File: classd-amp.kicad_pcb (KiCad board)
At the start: 4 copper layers, 80 parts, among them J1 POWER, Q1 IRF540N, Q2 IRF540N, Q3 IRF540N, Q4 IRF540N, Q5 2N3906, Q6 2N3904, U1 TL072, U2 TL072, U3 NE555P, U4 LT1016, U5 IR2184, U6 IR2184, U7 LM7812_TO220, U8 LM7805_TO220, U9 LM358

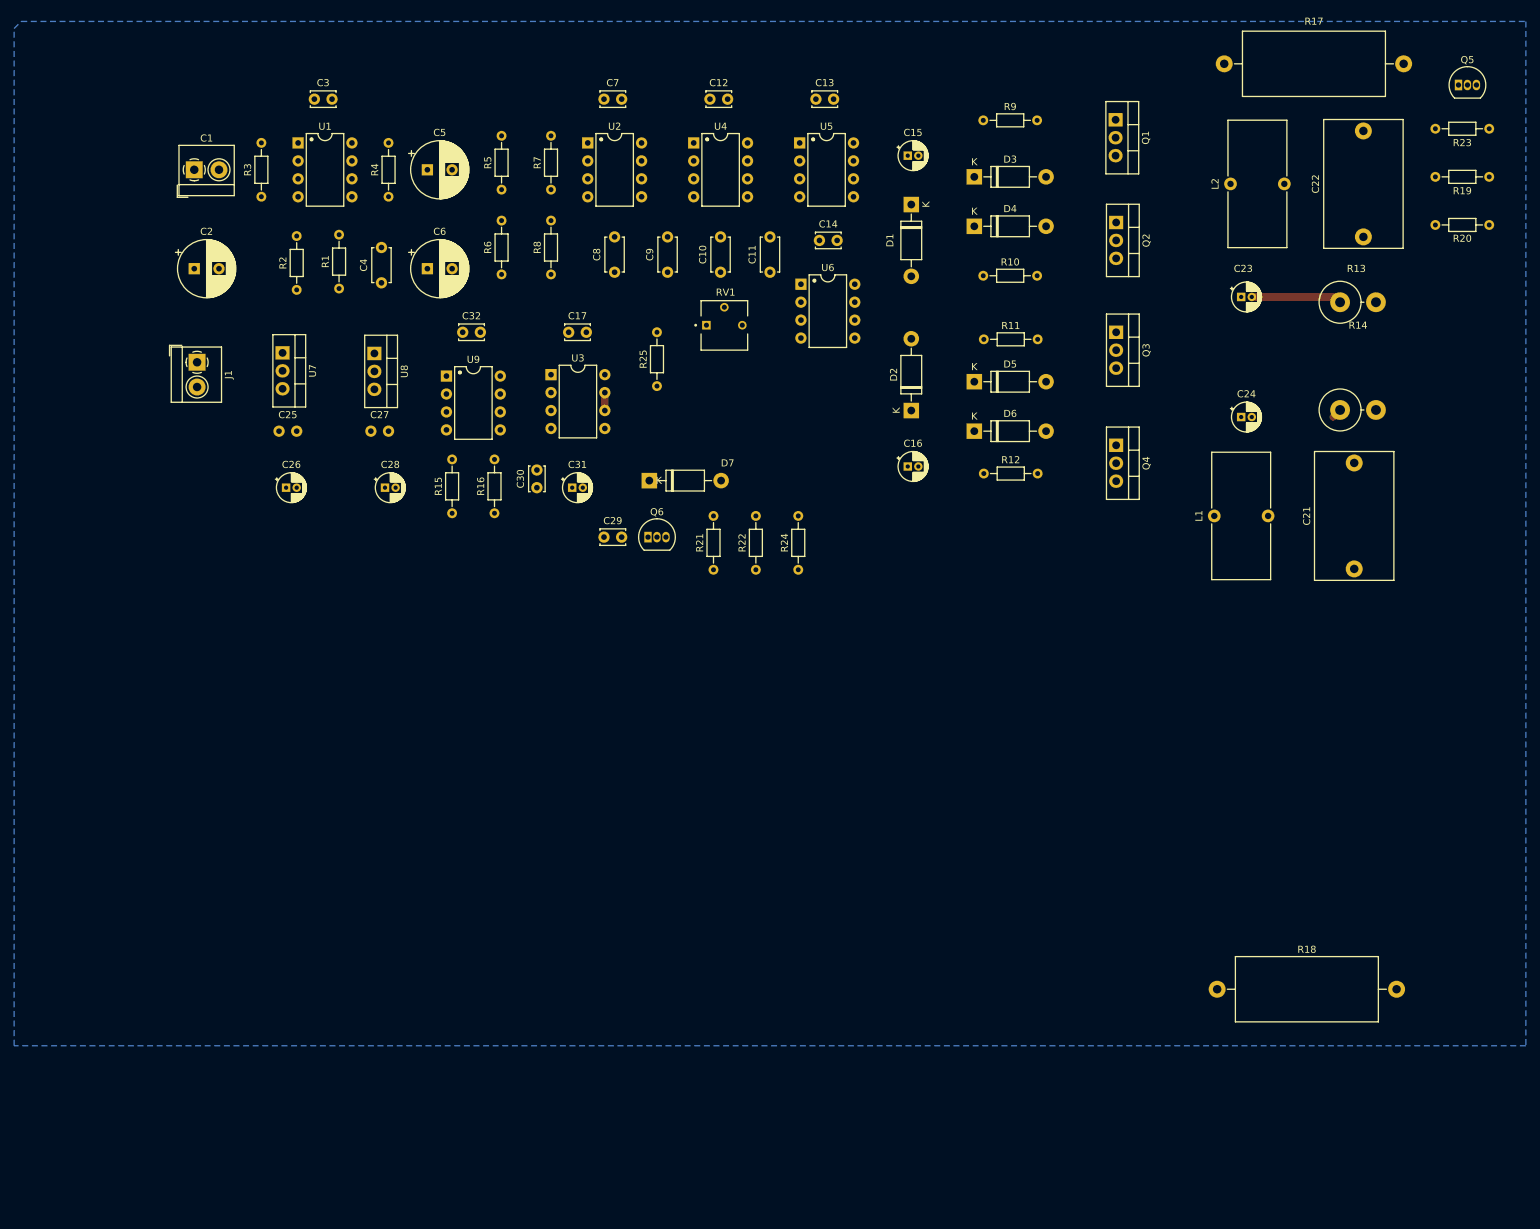
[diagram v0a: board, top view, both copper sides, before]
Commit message: Added right channel
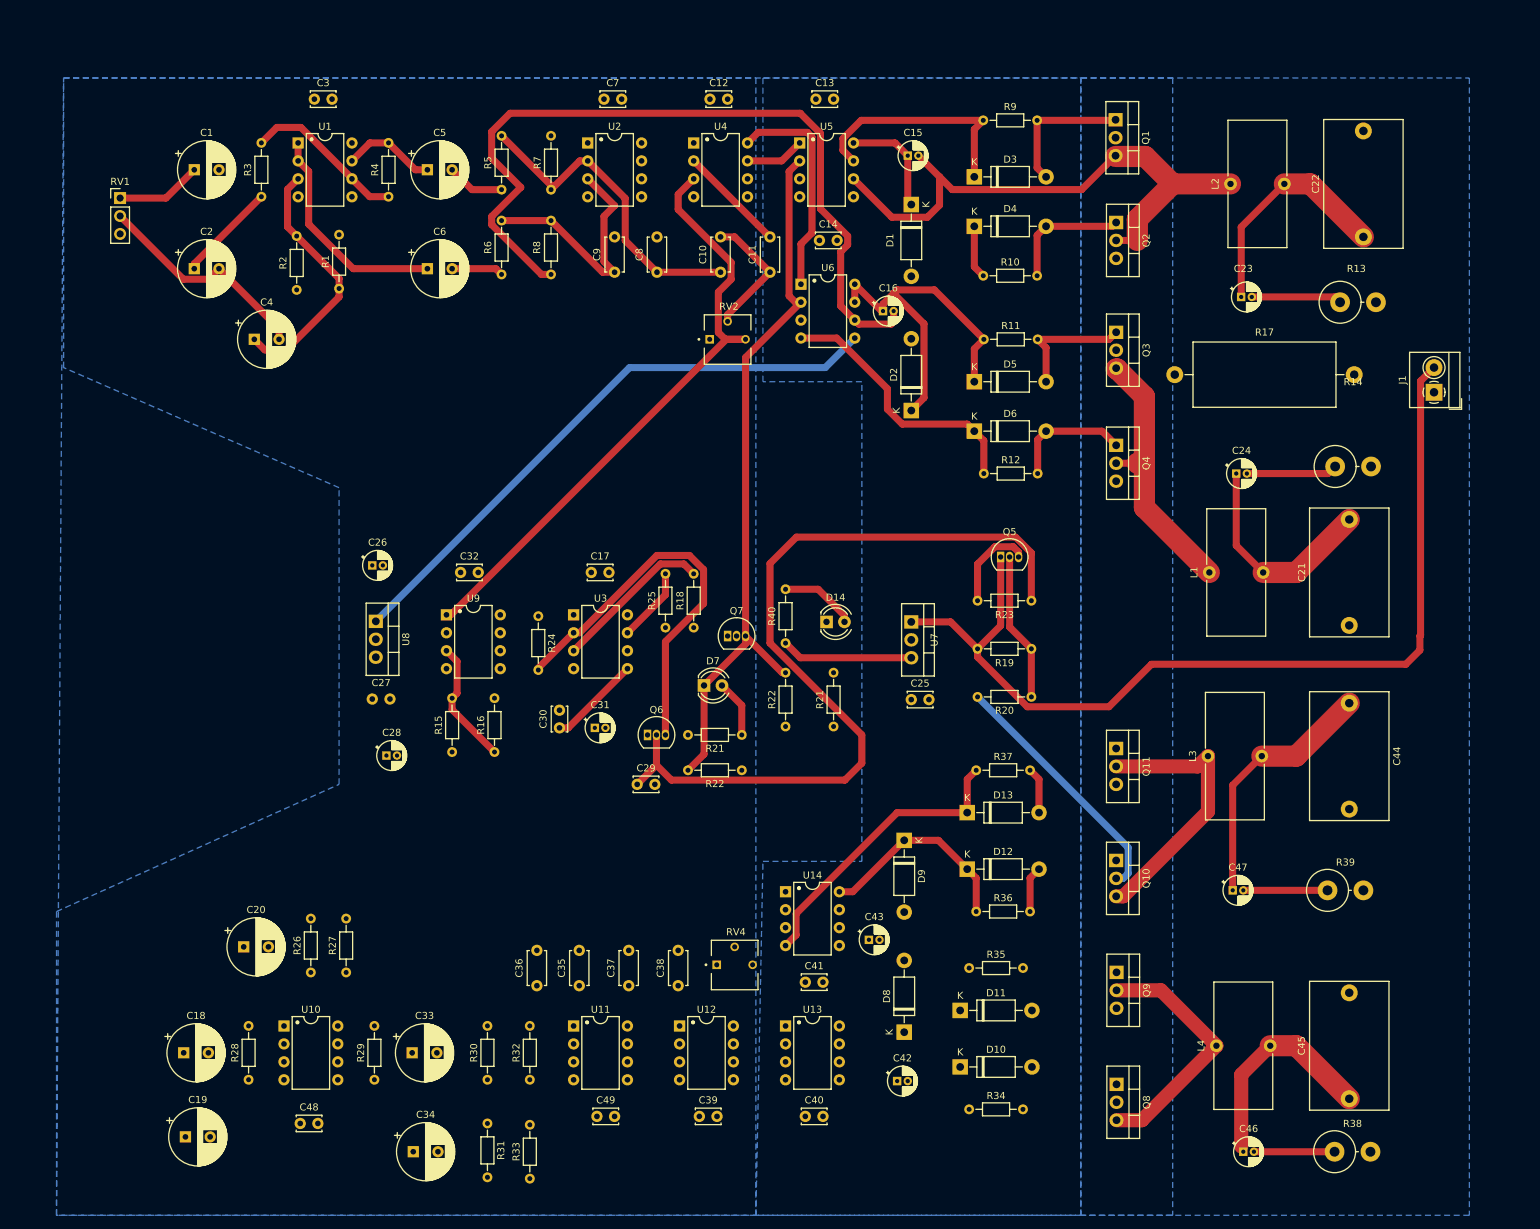
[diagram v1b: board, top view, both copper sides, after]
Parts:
- added C18: 22u, Capacitor_THT:CP_Radial_D8.0mm_P3.50mm, F.Cu at (46.0, 164.0)
- added C19: 22u, Capacitor_THT:CP_Radial_D8.0mm_P3.50mm, F.Cu at (46.2, 175.9)
- added C20: 22u, Capacitor_THT:CP_Radial_D8.0mm_P3.50mm, F.Cu at (54.5, 149.0)
- added C33: 22u, Capacitor_THT:CP_Radial_D8.0mm_P3.50mm, F.Cu at (78.3, 164.0)
- added C34: 22u, Capacitor_THT:CP_Radial_D8.0mm_P3.50mm, F.Cu at (78.5, 178.0)
- added C35: 1n, Capacitor_THT:C_Disc_D4.7mm_W2.5mm_P5.00mm, F.Cu at (102.0, 154.5)
- added C36: 1n, Capacitor_THT:C_Disc_D4.7mm_W2.5mm_P5.00mm, F.Cu at (96.0, 154.5)
- added C37: 1n, Capacitor_THT:C_Disc_D4.7mm_W2.5mm_P5.00mm, F.Cu at (109.0, 154.5)
- added C38: 1n, Capacitor_THT:C_Disc_D4.7mm_W2.5mm_P5.00mm, F.Cu at (116.0, 154.5)
- added C39: 100n, Capacitor_THT:C_Disc_D3.4mm_W2.1mm_P2.50mm, F.Cu at (119.0, 173.0)
- added C40: 100n, Capacitor_THT:C_Disc_D3.4mm_W2.1mm_P2.50mm, F.Cu at (134.0, 173.0)
- added C41: 100n, Capacitor_THT:C_Disc_D3.4mm_W2.1mm_P2.50mm, F.Cu at (134.0, 154.0)
- added C42: 1u, Capacitor_THT:CP_Radial_D4.0mm_P1.50mm, F.Cu at (147.0, 168.0)
- added C43: 1u, Capacitor_THT:CP_Radial_D4.0mm_P1.50mm, F.Cu at (143.0, 148.0)
- added C44: 1u, Capacitor_THT:C_Rect_L18.0mm_W11.0mm_P15.00mm_FKS3_FKP3, F.Cu at (211.0, 114.5)
- added C45: 1u, Capacitor_THT:C_Rect_L18.0mm_W11.0mm_P15.00mm_FKS3_FKP3, F.Cu at (211.0, 170.5)
- added C46: 10u, Capacitor_THT:CP_Radial_D4.0mm_P1.50mm, F.Cu at (196.0, 178.0)
- added C47: 10u, Capacitor_THT:CP_Radial_D4.0mm_P1.50mm, F.Cu at (194.5, 141.0)
- added C48: 100n, Capacitor_THT:C_Disc_D3.4mm_W2.1mm_P2.50mm, F.Cu at (62.5, 174.0)
- added C49: 100n, Capacitor_THT:C_Disc_D3.4mm_W2.1mm_P2.50mm, F.Cu at (104.5, 173.0)
- added D10: SB140, Diode_THT:D_DO-41_SOD81_P10.16mm_Horizontal, F.Cu at (155.9, 166.0)
- added D11: SB140, Diode_THT:D_DO-41_SOD81_P10.16mm_Horizontal, F.Cu at (155.9, 158.0)
- added D12: SB140, Diode_THT:D_DO-41_SOD81_P10.16mm_Horizontal, F.Cu at (156.9, 138.0)
- added D13: SB140, Diode_THT:D_DO-41_SOD81_P10.16mm_Horizontal, F.Cu at (156.9, 130.0)
- added D14: POWER, LED_THT:LED_D4.0mm, F.Cu at (137.0, 103.0)
- added D8: 1N4001, Diode_THT:D_DO-41_SOD81_P10.16mm_Horizontal, F.Cu at (148.0, 161.1)
- added D9: 1N4001, Diode_THT:D_DO-41_SOD81_P10.16mm_Horizontal, F.Cu at (148.0, 133.9)
- added L3: 33u, Inductor_THT:L_Toroid_Vertical_L17.8mm_W8.1mm_P7.62mm_Bourns_5700, F.Cu at (191.0, 122.0)
- added L4: 33u, Inductor_THT:L_Toroid_Vertical_L17.8mm_W8.1mm_P7.62mm_Bourns_5700, F.Cu at (192.2, 163.0)
- added Q10: IRF540N, Package_TO_SOT_THT:TO-220-3_Vertical, F.Cu at (178.0, 136.8)
- added Q11: IRF540N, Package_TO_SOT_THT:TO-220-3_Vertical, F.Cu at (178.0, 120.9)
- added Q7: 2N3904, Package_TO_SOT_THT:TO-92_Inline, F.Cu at (123.0, 105.0)
- added Q8: IRF540N, Package_TO_SOT_THT:TO-220-3_Vertical, F.Cu at (178.1, 168.5)
- added Q9: IRF540N, Package_TO_SOT_THT:TO-220-3_Vertical, F.Cu at (178.1, 152.6)
- added R21: 220, Resistor_THT:R_Axial_DIN0204_L3.6mm_D1.6mm_P7.62mm_Horizontal, F.Cu at (138.0, 117.8)
- added R22: 4.7k, Resistor_THT:R_Axial_DIN0204_L3.6mm_D1.6mm_P7.62mm_Horizontal, F.Cu at (131.2, 117.8)
- added R26: 22k, Resistor_THT:R_Axial_DIN0204_L3.6mm_D1.6mm_P7.62mm_Horizontal, F.Cu at (64.0, 152.6)
- added R27: 22k, Resistor_THT:R_Axial_DIN0204_L3.6mm_D1.6mm_P7.62mm_Horizontal, F.Cu at (69.0, 152.6)
- added R28: 47k, Resistor_THT:R_Axial_DIN0204_L3.6mm_D1.6mm_P7.62mm_Horizontal, F.Cu at (55.2, 167.8)
- added R29: 47k, Resistor_THT:R_Axial_DIN0204_L3.6mm_D1.6mm_P7.62mm_Horizontal, F.Cu at (73.0, 167.8)
- added R30: 3.3k, Resistor_THT:R_Axial_DIN0204_L3.6mm_D1.6mm_P7.62mm_Horizontal, F.Cu at (89.0, 167.8)
- added R31: 3.3k, Resistor_THT:R_Axial_DIN0204_L3.6mm_D1.6mm_P7.62mm_Horizontal, F.Cu at (89.0, 174.0)
- added R32: 100k, Resistor_THT:R_Axial_DIN0204_L3.6mm_D1.6mm_P7.62mm_Horizontal, F.Cu at (95.0, 167.8)
- added R33: 100k, Resistor_THT:R_Axial_DIN0204_L3.6mm_D1.6mm_P7.62mm_Horizontal, F.Cu at (95.0, 181.8)
- added R34: 4.7, Resistor_THT:R_Axial_DIN0204_L3.6mm_D1.6mm_P7.62mm_Horizontal, F.Cu at (157.2, 172.0)
- added R35: 4.7, Resistor_THT:R_Axial_DIN0204_L3.6mm_D1.6mm_P7.62mm_Horizontal, F.Cu at (157.2, 152.0)
- added R36: 4.7, Resistor_THT:R_Axial_DIN0204_L3.6mm_D1.6mm_P7.62mm_Horizontal, F.Cu at (158.2, 144.0)
- added R37: 4.7, Resistor_THT:R_Axial_DIN0204_L3.6mm_D1.6mm_P7.62mm_Horizontal, F.Cu at (158.2, 124.0)
- added R38: 10, Resistor_THT:R_Axial_DIN0614_L14.3mm_D5.7mm_P5.08mm_Vertical, F.Cu at (208.9, 178.0)
- added R39: 10, Resistor_THT:R_Axial_DIN0614_L14.3mm_D5.7mm_P5.08mm_Vertical, F.Cu at (207.9, 141.0)
- added R40: 1k, Resistor_THT:R_Axial_DIN0204_L3.6mm_D1.6mm_P7.62mm_Horizontal, F.Cu at (131.2, 106.0)
- added RV2: 1k, Potentiometer_THT:TRIM_3362P-1-253LF, F.Cu at (123.0, 63.0)
- added RV4: 1k, Potentiometer_THT:TRIM_3362P-1-253LF, F.Cu at (124.0, 151.5)
- added U10: TL072, PCM_Package_DIP_AKL:DIP-8_W7.62mm, F.Cu at (60.2, 160.2)
- added U11: TL072, PCM_Package_DIP_AKL:DIP-8_W7.62mm, F.Cu at (101.2, 160.2)
- added U12: LT1016, PCM_Package_DIP_AKL:DIP-8_W7.62mm, F.Cu at (116.2, 160.2)
- added U13: IR2184, PCM_Package_DIP_AKL:DIP-8_W7.62mm, F.Cu at (131.2, 160.2)
- added U14: IR2184, PCM_Package_DIP_AKL:DIP-8_W7.62mm, F.Cu at (131.2, 141.2)
- C1: footprint TerminalBlock_4Ucon:TerminalBlock_4Ucon_1x02_P3.50mm_Horizontal -> Capacitor_THT:CP_Radial_D8.0mm_P3.50mm
- C25: moved to F.Cu
- C4: value 1n -> 22u; footprint Capacitor_THT:C_Disc_D4.7mm_W2.5mm_P5.00mm -> Capacitor_THT:CP_Radial_D8.0mm_P3.50mm
- D7: value 1N4001 -> FAULT; footprint Diode_THT:D_DO-41_SOD81_P10.16mm_Horizontal -> LED_THT:LED_D4.0mm
- R18: value 0.5 -> 4.7k; footprint Resistor_THT:R_Axial_DIN0922_L20.0mm_D9.0mm_P25.40mm_Horizontal -> Resistor_THT:R_Axial_DIN0204_L3.6mm_D1.6mm_P7.62mm_Horizontal
- R19: value 2.2k -> 1.5k
- R21: value 1k -> 220
- R22: value 2.2k -> 4.7k
- R23: value 1k -> 4.7k
- RV1: value 1k -> 50k; footprint Potentiometer_THT:TRIM_3362P-1-253LF -> Connector_PinHeader_2.54mm:PinHeader_1x03_P2.54mm_Vertical
- moved J1 175.2 mm to (223.0, 70.5), turned to 90 degrees
- moved U7 96.8 mm to (149.0, 103.0)
- moved C25 94.9 mm to (149.0, 114.0), turned to 0 degrees
- moved Q5 93.1 mm to (161.7, 93.8)
- moved R19 93.1 mm to (158.4, 106.8)
- moved R20 93.1 mm to (166.0, 113.6)
- moved R23 93.1 mm to (158.4, 100.0)
- moved R18 90.1 mm to (118.2, 103.8), turned to 90 degrees
- moved RV1 87.4 mm to (37.0, 43.0)
- moved R17 44.6 mm to (211.7, 68.0)
- moved C27 37.9 mm to (75.2, 113.9)
- moved C28 37.9 mm to (74.7, 121.9)
- moved U8 37.9 mm to (73.2, 102.9)
- moved R24 37.4 mm to (96.2, 102.2), turned to -90 degrees
- moved C29 35.3 mm to (110.2, 126.0)
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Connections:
- net /LOUT+ renamed /Left Channel/LOUT+
- net /LOUT- renamed /Left Channel/LOUT-
- C1 pad 2: IN -> LIN
- C2 pad 1: Net-(U1A-+) -> Net-(C2-Pad1)
- C2 pad 2: IN -> Net-(C2-Pad2)
- C29 pad 1: Net-(D7-K) -> Net-(Q6-B)
- C4 pad 1: Net-(U1B--) -> Net-(U1A-+)
- C4 pad 2: Net-(C4-Pad2) -> Net-(C2-Pad2)
- C5 pad 1: Net-(C4-Pad2) -> Net-(C5-Pad1)
- D5 pad 1: Net-(D5-K) -> Net-(D2-K)
- D7 pad 1: Net-(D7-K) -> ~{SHUTDOWN}
- Q2 pad 3: DRIVE- -> GND
- Q4 pad 3: DRIVE- -> GND
- Q6 pad 2: Net-(D7-K) -> Net-(Q6-B)
- R11 pad 1: Net-(D5-K) -> Net-(D2-K)
- R18 pad 1: DRIVE- -> Net-(Q7-B)
- R18 pad 2: GND -> Net-(U3-Q)
- R21 pad 1: DRIVE- -> Net-(D7-A)
- R21 pad 2: Net-(D7-K) -> +5V
- R22 pad 1: Net-(D7-K) -> +5V
- R22 pad 2: GND -> ~{SHUTDOWN}
- R23 pad 2: Net-(D7-A) -> Net-(Q6-B)
- R3 pad 1: Net-(C1-Pad1) -> Net-(C2-Pad1)
- R4 pad 2: Net-(C4-Pad2) -> Net-(C5-Pad1)
- RV1 pad 1: unconnected-(RV1-Pad1) -> Net-(C1-Pad1)
- RV1 pad 2: Net-(C10-Pad2) -> Net-(C2-Pad2)
- RV1 pad 3: BIAS -> GND
- U1 pad 7: Net-(C4-Pad2) -> Net-(C5-Pad1)
- U3 pad 3: ~{SHUTDOWN} -> Net-(U3-Q)
- U6 pad 7: Net-(D5-K) -> Net-(D2-K)
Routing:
- net Net-(Q3-S): track 0.00 -> 151.9 mm
- net B+: track 255.5 -> 136.2 mm
- net Net-(Q6-B): track 0.00 -> 119.0 mm
- net ~{SHUTDOWN}: track 0.00 -> 102.5 mm
- net BIAS: track 0.00 -> 89.3 mm
- net Net-(Q1-S): track 0.00 -> 82.0 mm
- net Net-(Q6-C): track 0.00 -> 56.7 mm
- net Net-(D2-K): track 0.00 -> 52.8 mm
- net +12V: track 155.1 -> 103.1 mm
- net Net-(U2A--): track 0.00 -> 46.2 mm
- net Net-(D13-K): track 0.00 -> 41.8 mm
- net Net-(Q10-S): track 0.00 -> 39.4 mm
- net Net-(D6-K): track 0.00 -> 38.3 mm
- net /Right Channel/ROUT-: track 0.00 -> 36.2 mm
- net Net-(U1A-+): track 0.00 -> 36.1 mm
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- added copper zone on B.Cu, net +12V
- added copper zone on B.Cu, net +5V
- added copper zone on B.Cu, net DRIVE+
- added copper zone on In1.Cu, net GND
- removed copper zone on In1.Cu, net DRIVE+

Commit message: First prototype
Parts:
- added J2: Conn_Coaxial_x2, Connector_Audio:RCA_Stereo_Connector, F.Cu at (58.0, 106.0)
- added J3: LEFT, TerminalBlock_4Ucon:TerminalBlock_4Ucon_1x02_P3.50mm_Horizontal, F.Cu at (223.0, 73.5)
- added J4: RIGHT, TerminalBlock_4Ucon:TerminalBlock_4Ucon_1x02_P3.50mm_Horizontal, F.Cu at (222.9, 152.8)
- added REF**: MountingHole_3.2mm_M3, MountingHole:MountingHole_3.2mm_M3, F.Cu at (223.0, 42.0)
- added REF**: MountingHole_3.2mm_M3, MountingHole:MountingHole_3.2mm_M3, F.Cu at (54.0, 42.0)
- added REF**: MountingHole_3.2mm_M3, MountingHole:MountingHole_3.2mm_M3, F.Cu at (223.0, 167.0)
- added REF**: MountingHole_3.2mm_M3, MountingHole:MountingHole_3.2mm_M3, F.Cu at (54.0, 167.0)
- added RV3: 50k, Connector_PinHeader_2.54mm:PinHeader_1x03_P2.54mm_Vertical, F.Cu at (53.0, 132.5)
- C27: moved to F.Cu
- moved C26 57.2 mm to (129.5, 102.0)
- moved C19 48.4 mm to (70.5, 134.0)
- moved C28 45.9 mm to (95.5, 81.0)
- moved C1 45.9 mm to (60.5, 83.0)
- moved R23 42.9 mm to (122.8, 124.0), turned to 180 degrees
- moved RV1 40.7 mm to (53.0, 80.5)
- moved C2 37.8 mm to (70.5, 83.0)
- moved U8 36.6 mm to (102.1, 80.5)
- moved Q5 36.0 mm to (136.7, 119.7), turned to -90 degrees
- moved C27 33.7 mm to (95.5, 87.0), turned to 0 degrees
- moved C18 32.9 mm to (59.5, 134.0)
- moved C4 32.3 mm to (81.3, 83.0)
- moved C20 30.9 mm to (81.5, 134.0)
- moved L2 30.1 mm to (191.2, 71.0)
- moved C22 30.1 mm to (211.0, 78.5)
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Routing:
- net +5V: track 0.00 -> 362.3 mm
- net BIAS: track 89.3 -> 316.0 mm
- net Net-(Q8-S): track 35.9 -> 165.9 mm
- net +12V: track 103.1 -> 220.9 mm
- net DRIVE+: track 71.2 -> 176.2 mm
- net Net-(Q10-S): track 39.4 -> 132.2 mm
- net Net-(Q6-B): track 119.0 -> 27.2 mm
- net ~{SHUTDOWN}: track 102.5 -> 164.0 mm
- net Net-(D4-K): track 7.53 -> 57.2 mm
- net Net-(Q1-S): track 82.0 -> 125.9 mm
- net Net-(Q3-S): track 151.9 -> 194.8 mm
- net Net-(U4-+): track 15.3 -> 57.0 mm
- net Net-(U11A--): track 0.00 -> 40.3 mm
- net /Right Channel/ROUT-: track 36.2 -> 75.5 mm
- net Net-(D11-K): track 0.00 -> 37.8 mm
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- added copper zone on F.Cu, net GND
- added copper zone on In2.Cu, net GND
- removed copper zone on B.Cu, net +12V
- removed copper zone on B.Cu, net +5V
- removed copper zone on In2.Cu, net +5V
- removed copper zone on B.Cu, net DRIVE+
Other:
- board outline added: 177 x 133 mm
- board text added: "L VOL"
- board text added: "LEFT SPK"
- board text added: "LINE IN"
- board text added: "PWR+"
- board text added: "PWR-"
- board text added: "R VOL"
- board text added: "RIGHT SPK"
